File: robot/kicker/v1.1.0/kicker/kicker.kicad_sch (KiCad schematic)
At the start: 52 parts, among them J1 XT30PW-M, J2 1054052108, U1 LM1117-5.0, U2 LM1117-3.3, U3 ADUM7441

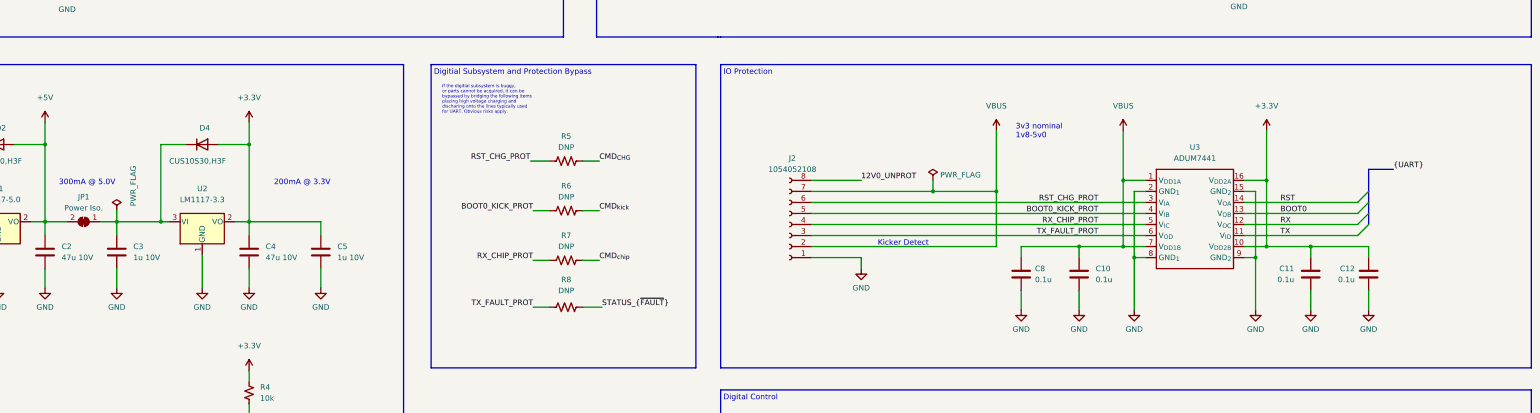
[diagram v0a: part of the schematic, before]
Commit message: address initial issues with v1.0.0
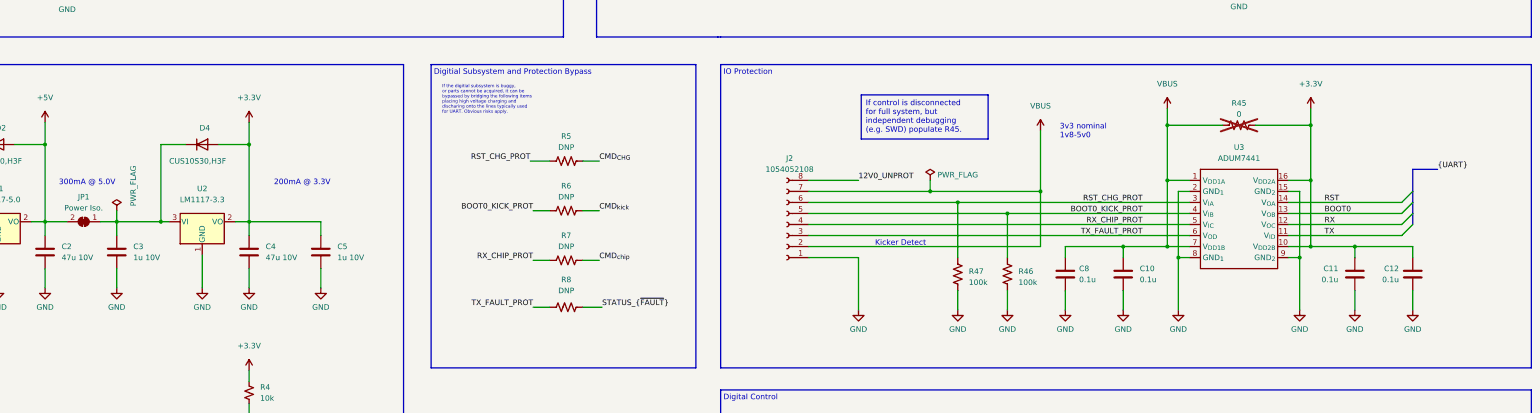
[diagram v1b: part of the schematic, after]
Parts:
- added R45: 0, Resistor_SMD:R_0603_1608Metric, symbol Device:R_US
- added R46, R47: 100k, Resistor_SMD:R_0603_1608Metric, symbol Device:R_US
- JP1: footprint Jumper:SolderJumper-2_P1.3mm_Bridged_RoundedPad1.0x1.5mm -> AT-BoardFeatures:SolderJumper-2_2.0x1.2mm_Closed
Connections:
- net +3V3: now also R45.2
- net BOOT0_KICK_PROT: now also R46.1
- net GND: now also R46.2, R47.2
- net RST_CHG_PROT: now also R47.1
- net VBUS: now also R45.1
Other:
- moved on the sheet: C10, C11, C12, C8, J2, U3
